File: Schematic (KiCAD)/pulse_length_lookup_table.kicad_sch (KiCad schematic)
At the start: 122 parts

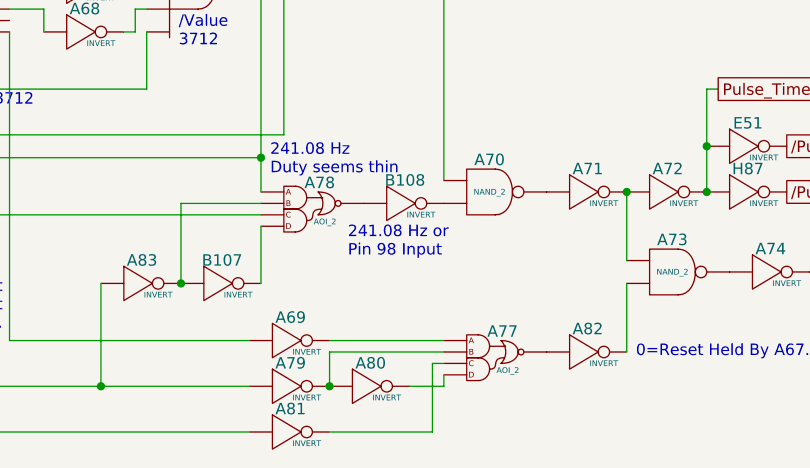
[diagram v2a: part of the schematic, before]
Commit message: - Updated all of the various And-OR-Invert gates to have consistent names.  - Added the schematic for CL3 / SL3 GPIO pins.  There are no surprises revealed by this.  - Finished up the CPU address decoding tracing.  - Added one of the 'artifact' counters from the pulse channels
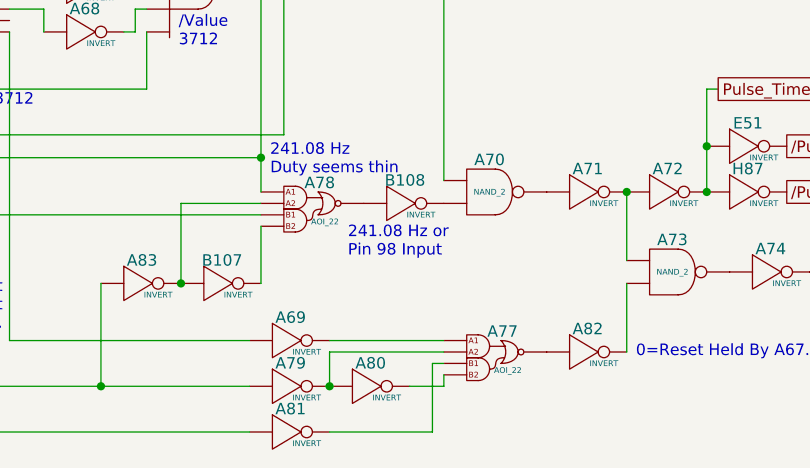
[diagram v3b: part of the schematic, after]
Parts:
- A77, A78: value AOI_2 -> AOI_22
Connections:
- net at B108. (X): now also A78. (X); no longer A70. (X)
- net at A71. (X): now also A72. (X), A73. (X); no longer A70. (X)
- net at C16. (X): now also D47. (X); no longer C15. (X)
- net at D45. (X): now also D46. (X); no longer C16. (X)
- net at D47. (X): now also D48. (X); no longer C16. (X)
- net at D72. (X): now also C22. (X); no longer D71. (X)
- net at D92. (X): now also C26. (X); no longer D91. (X)
- net at C26. (X): now also C25. (X); no longer D92. (X)
- net at C18. (X): now also D51. (X); no longer C17. (X)
- net at D106. (X): now also C28. (X); no longer D105. (X)
- net at A58. (X): now also A57. (X), A66. (/Q7); no longer A59. (X)
- net at D66. (X): now also D65. (X); no longer C20. (X)
- net at A67. (/Q4): now also A65. (X)
- net at A66.7. (X): now also A66.4. (X); no longer A67. (/Q4)
- net at A68. (X): now also A66.4. (X); no longer A67. (/Q4)
- net at A66.6. (X): now also A66.4. (X); no longer A67. (/Q4)
- net at A69. (X): now also A77. (X); no longer A67. (/Q4)
- net at A65. (X): now also A64. (X); no longer A67. (/Q4)
- net at A66.4. (X): now also A66.5. (X), A78. (X); no longer A66.7. (X)
- net at D64. (X): now also C20. (X); no longer D63. (X)
- net at D76. (X): now also C22. (X); no longer D75. (X)
- net at D53. (X): now also C18. (X); no longer D54. (X)
- net at D96. (X): now also D95. (X); no longer C26. (X)
- net at A73. (X): now also A74. (X); no longer A82. (X)
- net at A74. (X): now also A75. (X); no longer A73. (X)
- net at D49. (X): now also C18. (X); no longer D50. (X)
- net at D55. (X): now also C18. (X); no longer D56. (X)
- net at D74. (X): now also D73. (X); no longer C22. (X)
- net at D70. (X): now also D69. (X); no longer C22. (X)
- net at D68. (X): now also D67. (X); no longer C22. (X)
- net at A77. (X): now also A82. (X); no longer A81. (X)
- net at A77. (X), A80. (X): now also A79. (X)
- net at D104. (X): now also C28. (X); no longer D103. (X)
- net at C28. (X): now also C27. (X); no longer D104. (X)
- net at D58. (X): now also C20. (X); no longer D57. (X)
- net at C20. (X): now also D62. (X); no longer D58. (X)
- net at A66.3. (X): now also A66. (/Q7); no longer A66.4. (X)
- net at D78. (X): now also C24. (X); no longer D77. (X)
- net at C24. (X): now also D88. (X); no longer D78. (X)
- net at D102. (X): now also C28. (X); no longer D101. (X)
- net at D51. (X): now also D52. (X); no longer C18. (X)
- net at D100. (X): now also C26. (X); no longer D99. (X)
- net at D60. (X): now also C20. (X); no longer D59. (X)
- net at D84. (X): now also D83. (X); no longer C24. (X)
- net at D86. (X): now also C24. (X); no longer D85. (X)
- net at D82. (X): now also D81. (X); no longer C24. (X)
- net at D80. (X): now also D79. (X); no longer C24. (X)
- net at D90. (X): now also C26. (X); no longer D89. (X)
- net at A60. (X): now also A56. (X); no longer A61. (X)
- net at D94. (X): now also C26. (X); no longer D93. (X)
- net at A66.2. (X): now also A66.5. (X); no longer A66. (/Q7)
- net at D98. (X): now also D97. (X); no longer C26. (X)
- new net: A70. (X), B108. (X)
- new net: A70. (X), A71. (X)
- new net: C15. (X), C16. (X)
- new net: C16. (X), D45. (X)
- new net: D71. (X), D72. (X)
- new net: D91. (X), D92. (X)
- new net: C17. (X), C18. (X)
- new net: D105. (X), D106. (X)
- new net: A58. (X), A59. (X)
- new net: C20. (X), D66. (X)
- new net: A66.7. (X), A67. (/Q4)
- new net: A67. (/Q4), A68. (X)
- new net: A66.6. (X), A67. (/Q4)
- new net: A67. (/Q4), A69. (X)
- new net: A66. (/Q7), A67. (/Q4)
- new net: D63. (X), D64. (X)
- new net: D75. (X), D76. (X)
- new net: D53. (X), D54. (X)
- new net: C26. (X), D96. (X)
- new net: A73. (X), A82. (X)
- new net: D49. (X), D50. (X)
- new net: A64. (X), A66.4. (X), A66.5. (X)
- new net: D55. (X), D56. (X)
- new net: C21. (X), C22. (X)
- new net: C22. (X), D74. (X)
- new net: C22. (X), D70. (X)
- new net: C22. (X), D68. (X)
- new net: A77. (X), A81. (X)
- new net: A77. (X), A80. (X)
- new net: D103. (X), D104. (X)
- new net: D57. (X), D58. (X)
- new net: D61. (X), D62. (X)
- new net: A66.3. (X), A66.4. (X)
- new net: D77. (X), D78. (X)
- new net: C23. (X), C24. (X)
- new net: C19. (X), C20. (X)
- new net: A55. (/Q), A56. (X), A57. (X)
- new net: B43. (X), B44. (X)
- new net: B42. (X), B43. (X)
- new net: D101. (X), D102. (X)
- new net: C10. (X), D38. (Ripple_Out)
- new net: C10. (X), C9. (X)
- new net: D100. (X), D99. (X)
- new net: D59. (X), D60. (X)
- new net: D38. (Ripple_Out), D39. (Ripple_Out)
- new net: C24. (X), D84. (X)
- new net: D85. (X), D86. (X)
- new net: C11. (Ripple_Out), C12. (Ripple_Out)
- new net: B42. (X), C11. (Ripple_Out)
- new net: D87. (X), D88. (X)
- new net: C24. (X), D82. (X)
- new net: C24. (X), D80. (X)
- new net: D89. (X), D90. (X)
- new net: C8. (X), C9. (X)
- new net: A60. (X), A61. (X)
- new net: D93. (X), D94. (X)
- new net: A66. (/Q7), A66.2. (X)
- new net: A78. (X), A83. (X), B107. (X)
- new net: C26. (X), D98. (X)
